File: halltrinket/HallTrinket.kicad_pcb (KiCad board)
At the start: 2 copper layers, 32 parts, among them P1H1 CONN_1, P1H2 CONN_1, P1H3 CONN_1, P2H1 CONN_1, P2H2 CONN_1, P2H3 CONN_1, P3H1 CONN_1, P3H2 CONN_1, P3H3 CONN_1, P4H1 CONN_1, P4H2 CONN_1, P4H3 CONN_1

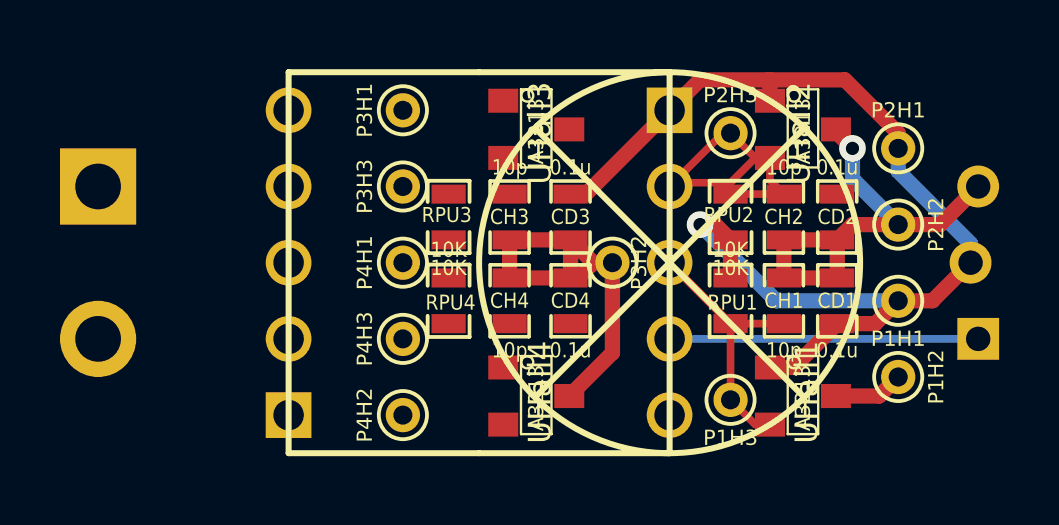
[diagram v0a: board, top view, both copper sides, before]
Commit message: Added OHW Logo.
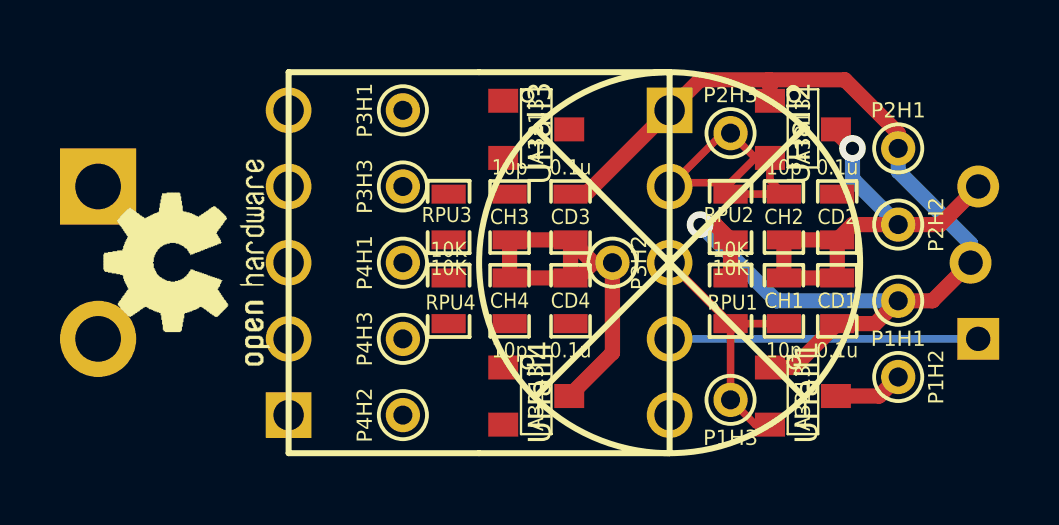
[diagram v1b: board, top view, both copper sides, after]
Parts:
- added G***: LOGO, OSHWLOGO0.3IN, F.Cu at (31.0, 54.6)

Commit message: Misc rework.
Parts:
- removed G***: LOGO, OSHWLOGO0.3IN
- removed P1H1, P1H2, P1H3, P2H1, P2H2, P2H3, P3H1, P3H2, P3H3, P4H1, P4H2, P4H3: CONN_1, PINTST
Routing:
- net VCC: track 37.6 -> 0.00 mm, vias 1 -> 0
- net VSS: track 32.2 -> 0.00 mm, vias 1 -> 0
- net /hallsensor1/hall1: track 11.7 -> 0.00 mm
- net /hallsensor2/hall2: track 10.9 -> 0.00 mm
- net /PB0: track 10.3 -> 0.00 mm
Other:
- net class Default: clearance 0.254 -> 0.2032
- net class PWR_Nets: clearance 0.254 -> 0.2032
- rule trace_clearance: 0.254 -> 0.2032
